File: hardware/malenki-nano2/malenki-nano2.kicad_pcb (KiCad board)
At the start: 2 copper layers, 19.1 x 24.1 mm, 22 parts, among them J1 Conn_01x02_Male, J2 Conn_01x04_Male, J5 Conn_01x02_Male, J6 Conn_01x02_Male, J7 Conn_01x02_Male, U1 A7105-MODULE, U2 HT7233, U3 ATtiny3217-M, U5 MX113L, U6 MX113L, U7 MX113L

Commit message: New funky version of the Nano2 board
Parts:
- added J3: Conn_01x02, malenki-nano:wirepad_2, B.Cu at (153.8, 73.8)
- J2: value Conn_01x04_Male -> Conn_01x03; footprint Connector_PinHeader_2.00mm:PinHeader_1x04_P2.00mm_Vertical -> Connector_PinHeader_2.00mm:PinHeader_1x03_P2.00mm_Vertical
- moved J2 2.35 mm to (153.9, 82.0)
- moved U1 0.28 mm to (145.9, 68.8)
- moved U3 0.21 mm to (144.3, 66.5)
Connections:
- J2 pad 1: GND -> /VLOGIC
- J2 pad 2: /VLOGIC -> TXDEBUG
- J2 pad 3: TXDEBUG -> UPDI
- U1 pad 4: BLINKY -> Net-(U1-Pad4)
- U3 pad 12: Net-(U3-Pad12) -> WEAPON2
- U3 pad 20: Net-(U3-Pad20) -> GND
- U3 pad 21: Net-(U3-Pad21) -> GND
- U3 pad 22: Net-(U3-Pad22) -> BLINKY
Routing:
- net WEAPON2: track 0.00 -> 13.3 mm, vias 0 -> 2
- net GND: track 29.4 -> 40.7 mm
- net BLINKY: track 3.03 -> 4.47 mm, vias 1 -> 0
- net SPI_SCK: track 9.24 -> 8.07 mm
- net MOTOR1R: track 9.36 -> 8.61 mm
- net /VLOGIC: track 37.1 -> 37.9 mm
- net MOTOR2R: track 9.05 -> 8.32 mm
- net MOTOR2F: track 9.50 -> 8.78 mm
- net TXDEBUG: track 34.7 -> 35.3 mm
- net SPI_SCS: track 10.0 -> 9.37 mm
- net SPI_SDIO: track 8.85 -> 8.25 mm
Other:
- board text added: "@markxr 2020"
- board text added: "LFT"
- board text added: "PWR"
- board text added: "RGT"
- board text removed: "@markxr-2019"
- board text removed: "LEFT"
- board text removed: "RGHT"

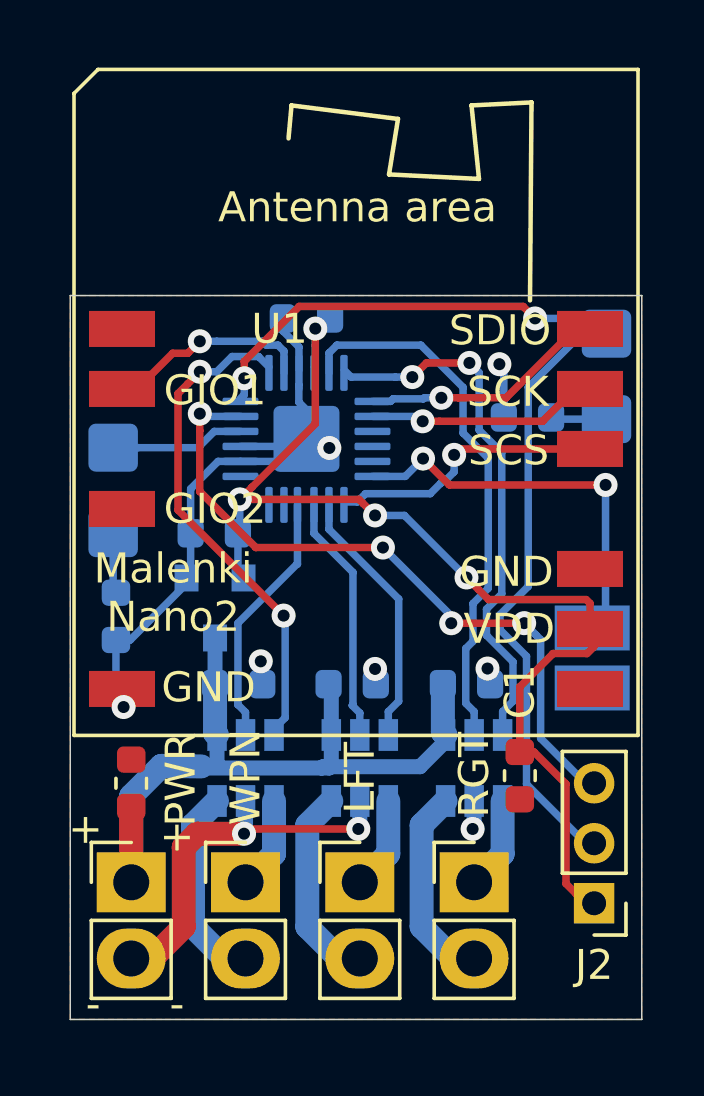
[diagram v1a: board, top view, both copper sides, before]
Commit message: move resistor to back side for assembly
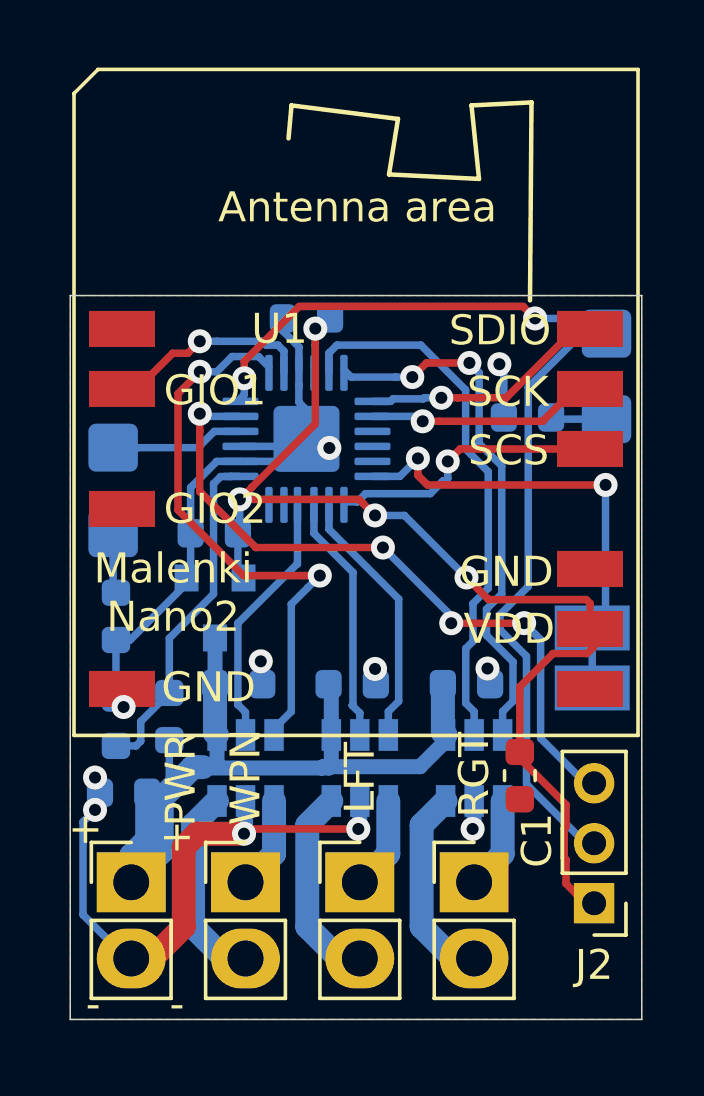
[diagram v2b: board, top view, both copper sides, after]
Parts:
- added R3: 33k, Resistor_SMD:R_0603_1608Metric, B.Cu at (139.7, 75.8)
- added R4: 10k, Resistor_SMD:R_0603_1608Metric, B.Cu at (137.9, 75.9)
- C2: moved to B.Cu
- moved C2 0.41 mm to (138.2, 78.3), turned to 180 degrees
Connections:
- J3 pad 2: GND -> WEAPON2
- U3 pad 19: Net-(U3-Pad19) -> VSENSE
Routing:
- net VSENSE: track 0.00 -> 11.3 mm
- net GND: track 40.7 -> 48.1 mm, vias 9 -> 11
- net MOTOR1F: track 16.7 -> 19.1 mm
- net WEAPON2: track 13.3 -> 15.7 mm
- net VBAT: track 26.5 -> 28.7 mm

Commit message: move around again
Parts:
- D1, D2: footprint LED_SMD:LED_1206_3216Metric_Castellated -> LED_SMD:LED_0805_2012Metric_Castellated
- U3: value ATtiny3217-M -> ATtiny1617-M
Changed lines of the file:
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@@
   )
   (layers
-    (0 "F.Cu" signal hide)
+    (0 "F.Cu" signal)
     (31 "B.Cu" signal)
     (32 "B.Adhes" user)
-    (33 "F.Adhes" user)
+    (33 "F.Adhes" user hide)
     (34 "B.Paste" user)
-    (35 "F.Paste" user)
+    (35 "F.Paste" user hide)
     (36 "B.SilkS" user)
-    (37 "F.SilkS" user)
+    (37 "F.SilkS" user hide)
     (38 "B.Mask" user)
-    (39 "F.Mask" user)
+    (39 "F.Mask" user hide)
     (40 "Dwgs.User" user)
     (41 "Cmts.User" user)
@@
     (visible_elements FFFDFF7F)
     (pcbplotparams
-      (layerselection 0x010fc_ffffffff)
+      (layerselection 0x110fc_ffffffff)
       (usegerberextensions false)
       (usegerberattributes false)
@@
     (add_net "WEAPON2")
   )
+  (module "LED_SMD:LED_0805_2012Metric_Castellated" (layer "B.Cu")
+    (at 154.273 64.417 90)
+    (descr "LED SMD 0805 (2012 Metric), castellated end terminal, IPC_7351 nominal, (Body size source: https://docs.google.com/spreadsheets/d/1BsfQQcO9C6DZCsRaXUlFlo91Tg2WpOkGARC1WS5S8t0/edit?usp=sharing), generated with kicad-footprint-generator")
+    (tags "LED castellated")
+    (attr smd)
+    (fp_text reference "D2" (at -2.893 -0.4125 180) (layer "B.SilkS")
+      (effects (font (size 1 1) (thickness 0.15)) (justify mirror))
+    )
+    (fp_text value "LED Red" (at 0 -1.6 90) (layer "B.Fab")
+      (effects (font (size 1 1) (thickness 0.15)) (justify mirror))
+    )
+    (fp_text user "%R" (at 0 0 90) (layer "B.Fab")
+      (effects (font (size 0.5 0.5) (thickness 0.08)) (justify mirror))
+    )
+    (fp_line (start 1.88 -0.9) (end -1.88 -0.9) (layer "B.CrtYd") (width 0.05))
+    (fp_line (start 1.88 0.9) (end 1.88 -0.9) (layer "B.CrtYd") (width 0.05))
+    (fp_line (start -1.88 0.9) (end 1.88 0.9) (layer "B.CrtYd") (width 0.05))
+    (fp_line (start -1.88 -0.9) (end -1.88 0.9) (layer "B.CrtYd") (width 0.05))
+    (fp_line (start -1.885 -0.91) (end 1 -0.91) (layer "B.SilkS") (width 0.12))
+    (fp_line (start -1.885 0.91) (end -1.885 -0.91) (layer "B.SilkS") (width 0.12))
+    (fp_line (start 1 0.91) (end -1.885 0.91) (layer "B.SilkS") (width 0.12))
+    (fp_line (start 1 -0.6) (end 1 0.6) (layer "B.Fab") (width 0.1))
+    (fp_line (start -1 -0.6) (end 1 -0.6) (layer "B.Fab") (width 0.1))
+    (fp_line (start -1 0.3) (end -1 -0.6) (layer "B.Fab") (width 0.1))
+    (fp_line (start -0.7 0.6) (end -1 0.3) (layer "B.Fab") (width 0.1))
+    (fp_line (start 1 0.6) (end -0.7 0.6) (layer "B.Fab") (width 0.1))
+    (pad "2" smd roundrect (at 0.9625 0 90) (size 1.325 1.3) (layers "B.Cu" "B.Paste" "B.Mask") (roundrect_rratio 0.192308)
+      (net 6 "TXDEBUG"))
+    (pad "1" smd roundrect (at -0.9625 0 90) (size 1.325 1.3) (layers "B.Cu" "B.Paste" "B.Mask") (roundrect_rratio 0.192308)
+      (net 7 "Net-(D2-Pad1)"))
+    (model "${KISYS3DMOD}/LED_SMD.3dshapes/LED_0805_2012Metric_Castellated.wrl"
+      (at (xyz 0 0 0))
+      (scale (xyz 1 1 1))
+      (rotate (xyz 0 0 0))
+    )
+  )
+  (module "LED_SMD:LED_0805_2012Metric_Castellated" (layer "B.Cu")
+    (at 137.827 68.217 90)
+    (descr "LED SMD 0805 (2012 Metric), castellated end terminal, IPC_7351 nominal, (Body size source: https://docs.google.com/spreadsheets/d/1BsfQQcO9C6DZCsRaXUlFlo91Tg2WpOkGARC1WS5S8t0/edit?usp=sharing), generated with kicad-footprint-generator")
+    (tags "LED castellated")
+    (attr smd)
+    (fp_text reference "D1" (at 0 1.6 90) (layer "B.SilkS")
+      (effects (font (size 1 1) (thickness 0.15)) (justify mirror))
+    )
+    (fp_text value "LED Blue" (at 0 -1.6 90) (layer "B.Fab")
+      (effects (font (size 1 1) (thickness 0.15)) (justify mirror))
+    )
+    (fp_text user "%R" (at 0 0 90) (layer "B.Fab")
+      (effects (font (size 0.5 0.5) (thickness 0.08)) (justify mirror))
+    )
+    (fp_line (start 1.88 -0.9) (end -1.88 -0.9) (layer "B.CrtYd") (width 0.05))
+    (fp_line (start 1.88 0.9) (end 1.88 -0.9) (layer "B.CrtYd") (width 0.05))
+    (fp_line (start -1.88 0.9) (end 1.88 0.9) (layer "B.CrtYd") (width 0.05))
+    (fp_line (start -1.88 -0.9) (end -1.88 0.9) (layer "B.CrtYd") (width 0.05))
+    (fp_line (start -1.885 -0.91) (end 1 -0.91) (layer "B.SilkS") (width 0.12))
+    (fp_line (start -1.885 0.91) (end -1.885 -0.91) (layer "B.SilkS") (width 0.12))
+    (fp_line (start 1 0.91) (end -1.885 0.91) (layer "B.SilkS") (width 0.12))
+    (fp_line (start 1 -0.6) (end 1 0.6) (layer "B.Fab") (width 0.1))
+    (fp_line (start -1 -0.6) (end 1 -0.6) (layer "B.Fab") (width 0.1))
+    (fp_line (start -1 0.3) (end -1 -0.6) (layer "B.Fab") (width 0.1))
+    (fp_line (start -0.7 0.6) (end -1 0.3) (layer "B.Fab") (width 0.1))
+    (fp_line (start 1 0.6) (end -0.7 0.6) (layer "B.Fab") (width 0.1))
+    (pad "2" smd roundrect (at 0.9625 0 90) (size 1.325 1.3) (layers "B.Cu" "B.Paste" "B.Mask") (roundrect_rratio 0.192308)
+      (net 4 "BLINKY"))
+    (pad "1" smd roundrect (at -0.9625 0 90) (size 1.325 1.3) (layers "B.Cu" "B.Paste" "B.Mask") (roundrect_rratio 0.192308)
+      (net 5 "Net-(D1-Pad1)"))
+    (model "${KISYS3DMOD}/LED_SMD.3dshapes/LED_0805_2012Metric_Castellated.wrl"
+      (at (xyz 0 0 0))
+      (scale (xyz 1 1 1))
+      (rotate (xyz 0 0 0))
+    )
+  )
   (module "Resistor_SMD:R_0603_1608Metric" (layer "B.Cu")
     (at 137.922 75.946 90)
@@
       (effects (font (size 1 1) (thickness 0.15)) (justify mirror))
     )
-    (fp_text value "ATtiny3217-M" (at 0 -3.3 90) (layer "B.Fab")
+    (fp_text value "ATtiny1617-M" (at 0 -3.3 90) (layer "B.Fab")
       (effects (font (size 1 1) (thickness 0.15)) (justify mirror))
     )
@@
       (at (xyz 0 0 0))
       (scale (xyz 1 1 1))
-      (rotate (xyz 0 0 0))
-    )
-  )
-  (module "LED_SMD:LED_1206_3216Metric_Castellated" (layer "B.Cu")
-    (at 154.273 64.417 90)
-    (descr "LED SMD 1206 (3216 Metric), castellated end terminal, IPC_7351 nominal, (Body size source: http://www.tortai-tech.com/upload/download/2011102023233369053.pdf), generated with kicad-footprint-generator")
-    (tags "LED castellated")
-    (attr smd)
-    (fp_text reference "D2" (at -3.274 -0.0315 180) (layer "B.SilkS")
-      (effects (font (size 1 1) (thickness 0.15)) (justify mirror))
-    )
-    (fp_text value "LED Red" (at 0 -1.78 90) (layer "B.Fab")
-      (effects (font (size 1 1) (thickness 0.15)) (justify mirror))
-    )
-    (fp_text user "%R" (at 0 0 90) (layer "B.Fab")
-      (effects (font (size 0.8 0.8) (thickness 0.12)) (justify mirror))
-    )
-    (fp_line (start 2.48 -1.08) (end -2.48 -1.08) (layer "B.CrtYd") (width 0.05))
-    (fp_line (start 2.48 1.08) (end 2.48 -1.08) (layer "B.CrtYd") (width 0.05))
-    (fp_line (start -2.48 1.08) (end 2.48 1.08) (layer "B.CrtYd") (width 0.05))
-    (fp_line (start -2.48 -1.08) (end -2.48 1.08) (layer "B.CrtYd") (width 0.05))
-    (fp_line (start -2.485 -1.085) (end 1.6 -1.085) (layer "B.SilkS") (width 0.12))
-    (fp_line (start -2.485 1.085) (end -2.485 -1.085) (layer "B.SilkS") (width 0.12))
-    (fp_line (start 1.6 1.085) (end -2.485 1.085) (layer "B.SilkS") (width 0.12))
-    (fp_line (start 1.6 -0.8) (end 1.6 0.8) (layer "B.Fab") (width 0.1))
-    (fp_line (start -1.6 -0.8) (end 1.6 -0.8) (layer "B.Fab") (width 0.1))
-    (fp_line (start -1.6 0.4) (end -1.6 -0.8) (layer "B.Fab") (width 0.1))
-    (fp_line (start -1.2 0.8) (end -1.6 0.4) (layer "B.Fab") (width 0.1))
-    (fp_line (start 1.6 0.8) (end -1.2 0.8) (layer "B.Fab") (width 0.1))
-    (pad "2" smd roundrect (at 1.425 0 90) (size 1.6 1.65) (layers "B.Cu" "B.Paste" "B.Mask") (roundrect_rratio 0.15625)
-      (net 6 "TXDEBUG"))
-    (pad "1" smd roundrect (at -1.425 0 90) (size 1.6 1.65) (layers "B.Cu" "B.Paste" "B.Mask") (roundrect_rratio 0.15625)
-      (net 7 "Net-(D2-Pad1)"))
-    (model "${KISYS3DMOD}/LED_SMD.3dshapes/LED_1206_3216Metric_Castellated.wrl"
-      (at (xyz 0 0 0))
-      (scale (xyz 1 1 1))
-      (rotate (xyz 0 0 0))
-    )
-  )
-  (module "LED_SMD:LED_1206_3216Metric_Castellated" (layer "B.Cu")
-    (at 137.827 68.217 90)
-    (descr "LED SMD 1206 (3216 Metric), castellated end terminal, IPC_7351 nominal, (Body size source: http://www.tortai-tech.com/upload/download/2011102023233369053.pdf), generated with kicad-footprint-generator")
-    (tags "LED castellated")
-    (attr smd)
-    (fp_text reference "D1" (at 3.0025 0.0315 180) (layer "B.SilkS")
-      (effects (font (size 1 1) (thickness 0.15)) (justify mirror))
-    )
-    (fp_text value "LED Blue" (at 0 -1.78 90) (layer "B.Fab")
-      (effects (font (size 1 1) (thickness 0.15)) (justify mirror))
-    )
-    (fp_text user "%R" (at 0 0 90) (layer "B.Fab")
-      (effects (font (size 0.8 0.8) (thickness 0.12)) (justify mirror))
-    )
-    (fp_line (start 2.48 -1.08) (end -2.48 -1.08) (layer "B.CrtYd") (width 0.05))
-    (fp_line (start 2.48 1.08) (end 2.48 -1.08) (layer "B.CrtYd") (width 0.05))
-    (fp_line (start -2.48 1.08) (end 2.48 1.08) (layer "B.CrtYd") (width 0.05))
-    (fp_line (start -2.48 -1.08) (end -2.48 1.08) (layer "B.CrtYd") (width 0.05))
-    (fp_line (start -2.485 -1.085) (end 1.6 -1.085) (layer "B.SilkS") (width 0.12))
-    (fp_line (start -2.485 1.085) (end -2.485 -1.085) (layer "B.SilkS") (width 0.12))
-    (fp_line (start 1.6 1.085) (end -2.485 1.085) (layer "B.SilkS") (width 0.12))
-    (fp_line (start 1.6 -0.8) (end 1.6 0.8) (layer "B.Fab") (width 0.1))
-    (fp_line (start -1.6 -0.8) (end 1.6 -0.8) (layer "B.Fab") (width 0.1))
-    (fp_line (start -1.6 0.4) (end -1.6 -0.8) (layer "B.Fab") (width 0.1))
-    (fp_line (start -1.2 0.8) (end -1.6 0.4) (layer "B.Fab") (width 0.1))
-    (fp_line (start 1.6 0.8) (end -1.2 0.8) (layer "B.Fab") (width 0.1))
-    (pad "2" smd roundrect (at 1.425 0 90) (size 1.6 1.65) (layers "B.Cu" "B.Paste" "B.Mask") (roundrect_rratio 0.15625)
-      (net 4 "BLINKY"))
-    (pad "1" smd roundrect (at -1.425 0 90) (size 1.6 1.65) (layers "B.Cu" "B.Paste" "B.Mask") (roundrect_rratio 0.15625)
-      (net 5 "Net-(D1-Pad1)"))
-    (model "${KISYS3DMOD}/LED_SMD.3dshapes/LED_1206_3216Metric_Castellated.wrl"
-      (at (xyz 0 0 0))
-      (scale (xyz 1 1 1))
